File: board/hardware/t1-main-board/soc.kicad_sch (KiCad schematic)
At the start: 0 parts

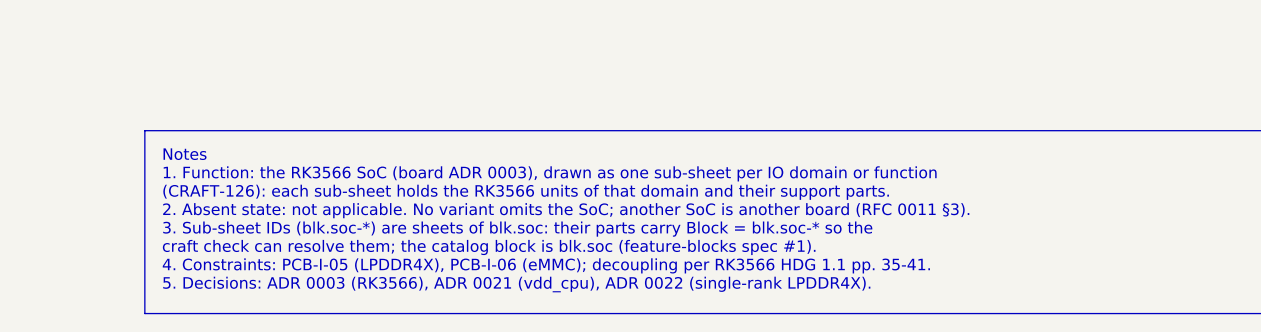
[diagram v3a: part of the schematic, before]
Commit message: vdd_cpu on the TPS62870Z4 (ADR 0026, placement v1.5)
ADR 0026 supersedes ADR 0023: TPS62870Z4WRXSR at I2C0 0x42 with the
Coilcraft XEL4012-920NE, 3 MHz, MODE/SYNC to ground with forced PWM by
register, differential sense from the 22 uF at the SoC. Output capacitance
sized at the 1.1 V devicetree cap for the 4.8 A worst-case step (peak
1.149 V, DC-bias effective values); 1800 MHz kept as a verification row.

Submodule at libs v0.3.2 (the RXS0016A land). BOM v1.18 item 8, power
tree v0.10, pinout v1 I2C0 note, feature blocks #13, placement v1.5.
Schematic regenerated, board rebuilt: 991 parts placed, 97.0 % board need,
factor 1.71, 244 capacitors within their bound, DRC 0 errors, ERC 0
errors, craft Q1 met, pcb tests pass, STEP exported (27 parts without a
model in KiCad's library, as before).

Co-Authored-By: Claude Opus 5.5 <noreply@anthropic.com>
Claude-Session: https://claude.ai/code/session_013P6pW9LdyEMFishwCcZGUr
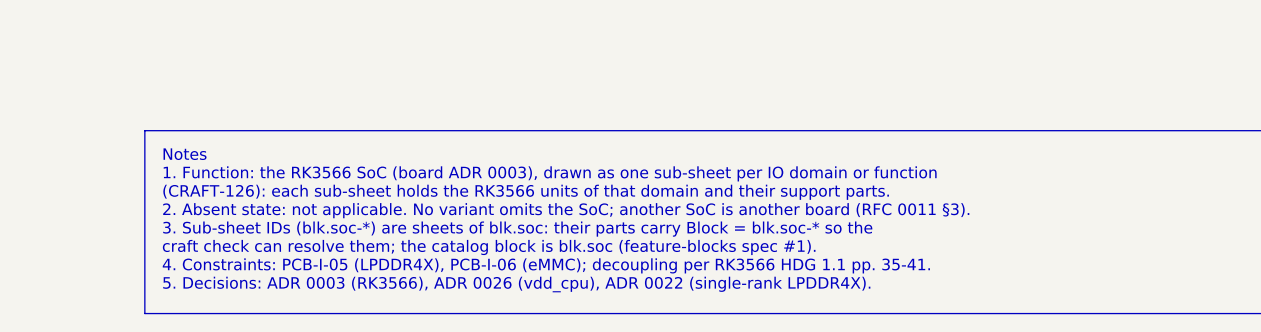
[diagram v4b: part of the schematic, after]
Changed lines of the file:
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@@
 (paper "A3")
 (title_block (title "SoC") (date "2026-10-25") (rev "A") (company "The OpenDAP Project") (comment 1 "blk.soc") (comment 2 "The RK3566 application processor, one sub-sheet per IO domain or function"))
-(text_box "Notes\n1. Function: the RK3566 SoC (board ADR 0003), drawn as one sub-sheet per IO domain or function\n   (CRAFT-126): each sub-sheet holds the RK3566 units of that domain and their support parts.\n2. Absent state: not applicable. No variant omits the SoC; another SoC is another board (RFC 0011 §3).\n3. Sub-sheet IDs (blk.soc-*) are sheets of blk.soc: their parts carry Block = blk.soc-* so the\n   craft check can resolve them; the catalog block is blk.soc (feature-blocks spec #1).\n4. Constraints: PCB-I-05 (LPDDR4X), PCB-I-06 (eMMC); decoupling per RK3566 HDG 1.1 pp. 35-41.\n5. Decisions: ADR 0003 (RK3566), ADR 0021 (vdd_cpu), ADR 0022 (single-rank LPDDR4X)." (exclude_from_sim no) (at 275.59 228.6 0) (size 129.54 20.32) (margins 1.905 1.905 1.905 1.905) (stroke (width 0) (type default)) (fill (type none)) (effects (font (size 1.27 1.27)) (justify left top)))
+(text_box "Notes\n1. Function: the RK3566 SoC (board ADR 0003), drawn as one sub-sheet per IO domain or function\n   (CRAFT-126): each sub-sheet holds the RK3566 units of that domain and their support parts.\n2. Absent state: not applicable. No variant omits the SoC; another SoC is another board (RFC 0011 §3).\n3. Sub-sheet IDs (blk.soc-*) are sheets of blk.soc: their parts carry Block = blk.soc-* so the\n   craft check can resolve them; the catalog block is blk.soc (feature-blocks spec #1).\n4. Constraints: PCB-I-05 (LPDDR4X), PCB-I-06 (eMMC); decoupling per RK3566 HDG 1.1 pp. 35-41.\n5. Decisions: ADR 0003 (RK3566), ADR 0026 (vdd_cpu), ADR 0022 (single-rank LPDDR4X)." (exclude_from_sim no) (at 275.59 228.6 0) (size 129.54 20.32) (margins 1.905 1.905 1.905 1.905) (stroke (width 0) (type default)) (fill (type none)) (effects (font (size 1.27 1.27)) (justify left top)))
 (sheet (at 41.91 30.48) (size 77.47 38.1) (exclude_from_sim no) (in_bom yes) (on_board yes) (dnp no) (fields_autoplaced yes) (stroke (width 0.1524) (type solid)) (fill (color 0 0 0 0.0000))
   (property "Sheetname" "SoC: PMU IO domains, clock, reset and SARADC" (at 41.91 29.7684 0) (effects (font (size 1.27 1.27)) (justify left bottom)))
